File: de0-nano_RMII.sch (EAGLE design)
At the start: 40 parts, among them U1 DP83848, X1 1-227161-2

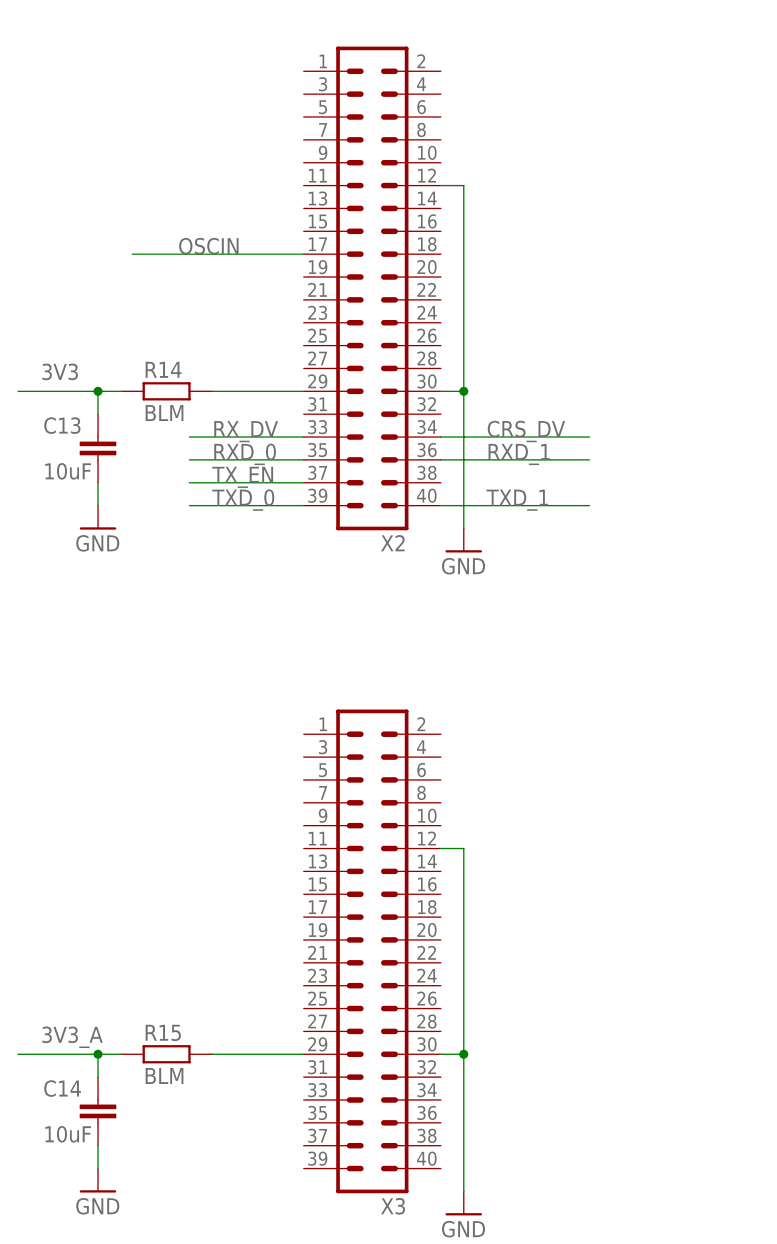
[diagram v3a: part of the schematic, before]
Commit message: removed some pads on connector
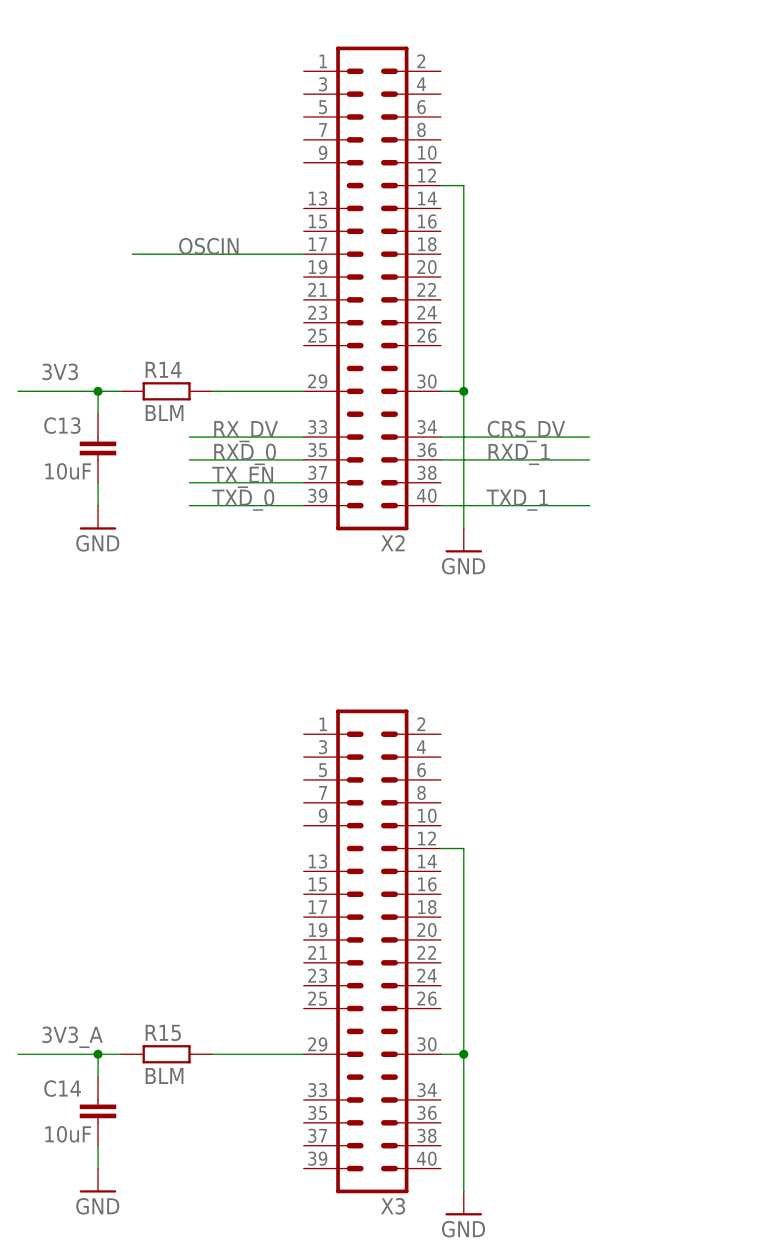
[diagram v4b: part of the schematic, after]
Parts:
- X2, X3: device con-lstb:MA20-2 -> con-lstb:MA20-2_ALT
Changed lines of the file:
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@@
 <?xml version="1.0" encoding="utf-8"?>
 <!DOCTYPE eagle SYSTEM "eagle.dtd">
-<eagle version="7.6.0">
+<eagle version="8.0.2">
 <drawing>
 <settings>
@@
 <setting verticaltext="up"/>
 </settings>
-<grid distance="0.05" unitdist="inch" unit="inch" style="lines" multiple="1" display="no" altdistance="0.01" altunitdist="inch" altunit="inch"/>
+<grid distance="0.1" unitdist="inch" unit="inch" style="lines" multiple="1" display="no" altdistance="0.01" altunitdist="inch" altunit="inch"/>
 <layers>
 <layer number="1" name="Top" color="4" fill="1" visible="no" active="no"/>
@@
 <part name="GND1" library="supply1" deviceset="GND" device=""/>
 <part name="X6" library="con-lstb" deviceset="MA13-2" device=""/>
-<part name="X2" library="con-lstb" deviceset="MA20-2" device=""/>
-<part name="X3" library="con-lstb" deviceset="MA20-2" device=""/>
+<part name="X2" library="con-lstb" deviceset="MA20-2_ALT" device=""/>
+<part name="X3" library="con-lstb" deviceset="MA20-2_ALT" device=""/>
 <part name="X7" library="seeed_connector" deviceset="RJ45-HR911105A" device="-HR911105A"/>
 <part name="U1" library="national-semiconductor" deviceset="DP83848" device=""/>

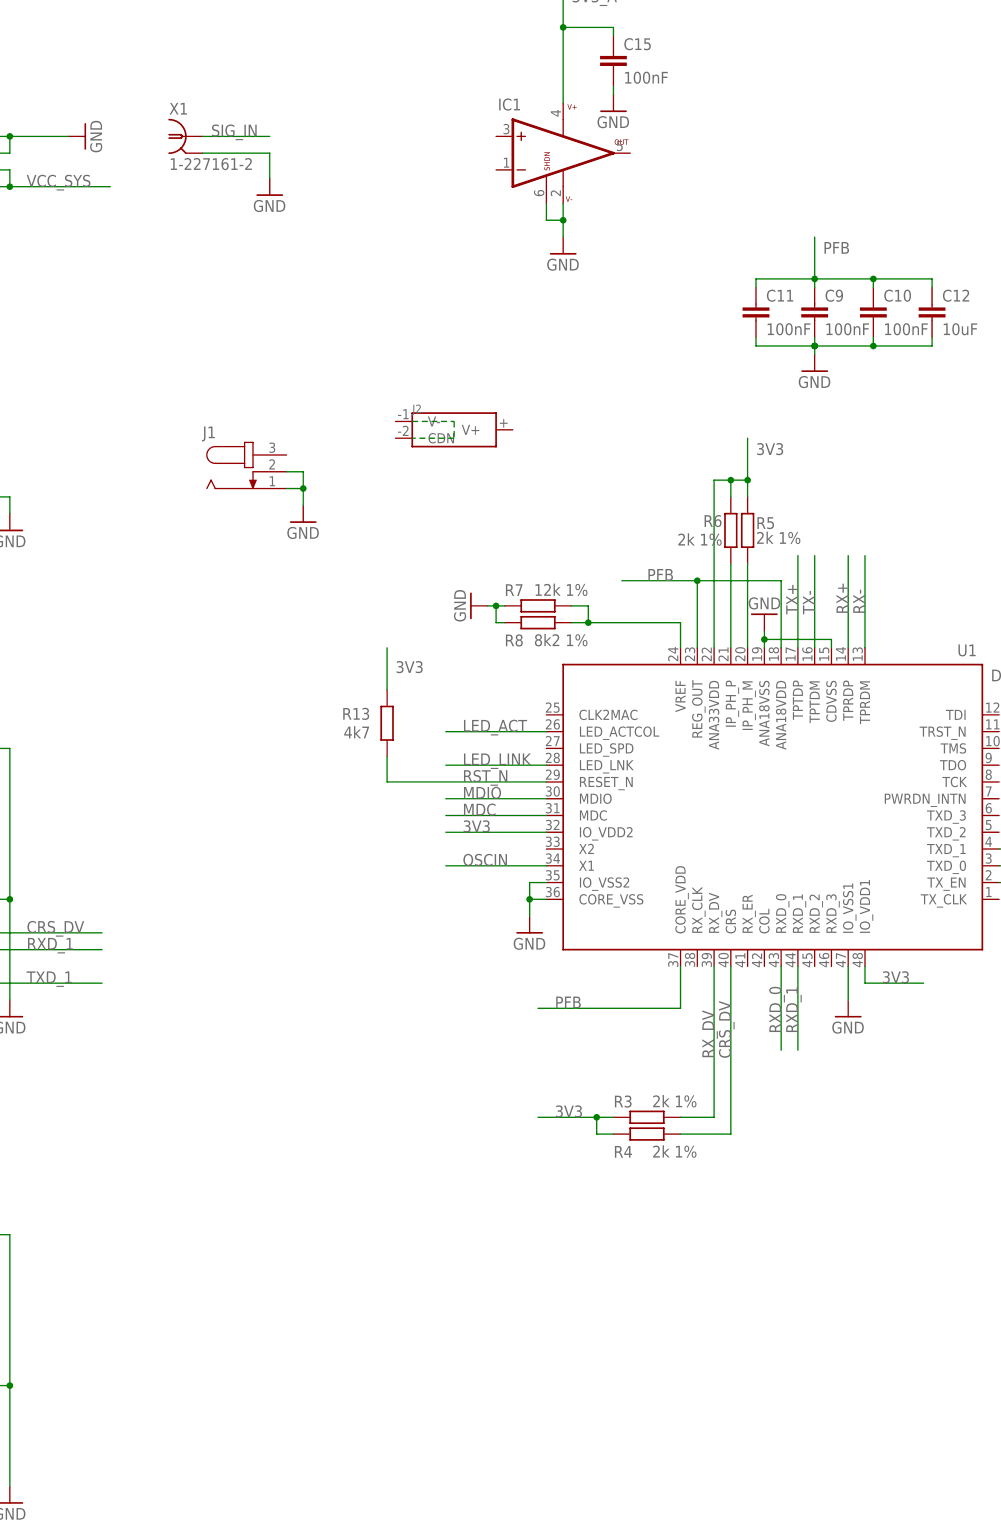
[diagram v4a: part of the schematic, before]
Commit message: added external power and DAC
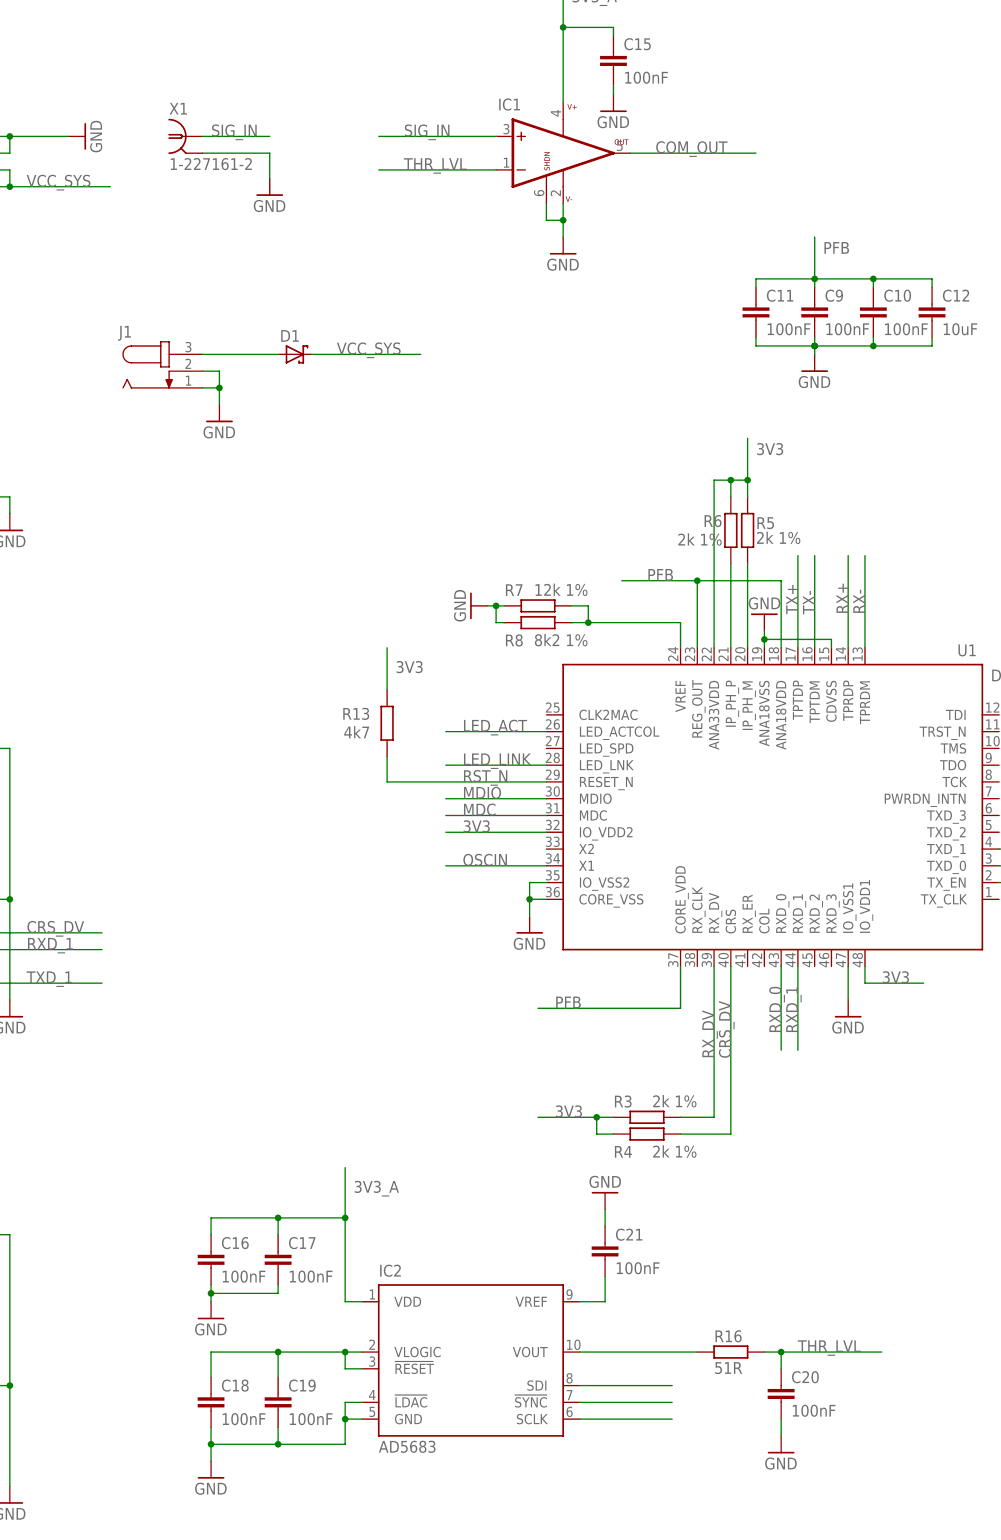
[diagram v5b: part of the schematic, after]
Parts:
- removed J2: (no value), seeed_connector:JACK-3P-2.5MM-2.5MM
- added C16, C17, C18, C19, C20, C21: 100nF, resistor:C-EUC0603
- added D1: (no value), diode:SCHOTTKY-DIODESMC
- added IC2: AD5683, analog-devices:AD5683
- added R16: 51R, resistor:R-EU_R0603
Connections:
- new net COM_OUT: IC1.OUT
- new net N$10: IC2.SDI
- new net N$11: IC2.!SYNC
- new net N$12: IC2.SCLK
- new net N$13: C21.1, IC2.VREF
- new net N$2: C18.1, C19.1, IC2.!RESET, IC2.VLOGIC
- new net N$8: IC2.VOUT, R16.1
- new net THR_LVL: C20.1, IC1.-IN, R16.2
- new net V_RAW: D1.A, J1.3
- net 3V3_A: now also C16.1, C17.1, IC2.VDD
- net GND: now also C16.2, C17.2, C18.2, C19.2, C20.2, C21.2, IC2.!LDAC, IC2.GND
- net SIG_IN: now also IC1.+IN
- net VCC_SYS: now also D1.C
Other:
- moved on the sheet: J1

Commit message: almost done
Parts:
- added R17: 4k7, resistor:R-EU_R0603
- X6: device con-lstb:MA13-2 -> con-lstb:MA13-2_ALT
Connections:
- net N$2 renamed VLOGIC
- removed net N$10: IC2.SDI
- removed net N$11: IC2.!SYNC
- removed net N$12: IC2.SCLK
- new net DAC_CLK: IC2.SCLK, X3.5
- new net DAC_NCS: IC2.!SYNC, R17.2, X3.7
- new net DAC_SDI: IC2.SDI, X3.6
- net 3V3_A: now also R17.1
- net COM_OUT: now also X3.13
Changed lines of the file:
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@@
 <?xml version="1.0" encoding="utf-8"?>
 <!DOCTYPE eagle SYSTEM "eagle.dtd">
-<eagle version="7.6.0">
+<eagle version="8.0.2">
 <drawing>
 <settings>
@@
 <part name="X1" library="con-coax" deviceset="?227161*" device="1-" technology="-2"/>
 <part name="GND1" library="supply1" deviceset="GND" device=""/>
-<part name="X6" library="con-lstb" deviceset="MA13-2" device=""/>
+<part name="X6" library="con-lstb" deviceset="MA13-2_ALT" device=""/>
 <part name="X2" library="con-lstb" deviceset="MA20-2_ALT" device=""/>
 <part name="X3" library="con-lstb" deviceset="MA20-2_ALT" device=""/>
@@
 <part name="C21" library="resistor" deviceset="C-EU" device="C0603" value="100nF"/>
 <part name="GND25" library="supply1" deviceset="GND" device=""/>
+<part name="R17" library="resistor" deviceset="R-EU_" device="R0603" value="4k7"/>
 </parts>
 <sheets>
@@
 </instance>
 <instance part="GND25" gate="1" x="146.05" y="71.12" rot="R180"/>
+<instance part="R17" gate="G$1" x="17.78" y="80.01" smashed="yes" rot="R270">
+<attribute name="NAME" x="15.24" y="82.3214" size="1.778" layer="95" rot="R180"/>
+<attribute name="VALUE" x="15.24" y="79.502" size="1.778" layer="96" rot="R180"/>
+</instance>
 </instances>
 <busses>
@@
 <junction x="106.68" y="67.31"/>
 </segment>
+<segment>
+<pinref part="R17" gate="G$1" pin="1"/>
+<wire x1="17.78" y1="85.09" x2="17.78" y2="93.98" width="0.1524" layer="91"/>
+<label x="19.05" y="88.9" size="1.778" layer="95"/>
+</segment>
 </net>
 <net name="N$1" class="0">
@@
 <label x="153.67" y="228.6" size="1.778" layer="95"/>
 </segment>
+<segment>
+<pinref part="X3" gate="G$1" pin="13"/>
+<wire x1="38.1" y1="62.23" x2="17.78" y2="62.23" width="0.1524" layer="91"/>
+<label x="22.86" y="62.23" size="1.778" layer="95"/>
+</segment>
 </net>
 <net name="V_RAW" class="0">
@@
 </segment>
 </net>
-<net name="N$2" class="0">
+<net name="VLOGIC" class="0">
 <segment>
 <pinref part="IC2" gate="G$1" pin="!RESET"/>
@@
 </segment>
 </net>
-<net name="N$10" class="0">
+<net name="DAC_SDI" class="0">
 <segment>
 <pinref part="IC2" gate="G$1" pin="SDI"/>
-<wire x1="142.24" y1="41.91" x2="156.21" y2="41.91" width="0.1524" layer="91"/>
-</segment>
-</net>
-<net name="N$11" class="0">
+<wire x1="142.24" y1="41.91" x2="158.75" y2="41.91" width="0.1524" layer="91"/>
+<label x="144.78" y="41.91" size="1.778" layer="95"/>
+</segment>
+<segment>
+<pinref part="X3" gate="G$1" pin="6"/>
+<wire x1="53.34" y1="72.39" x2="66.04" y2="72.39" width="0.1524" layer="91"/>
+<label x="55.88" y="72.39" size="1.778" layer="95"/>
+</segment>
+</net>
+<net name="DAC_NCS" class="0">
 <segment>
 <pinref part="IC2" gate="G$1" pin="!SYNC"/>
-<wire x1="142.24" y1="39.37" x2="156.21" y2="39.37" width="0.1524" layer="91"/>
-</segment>
-</net>
-<net name="N$12" class="0">
+<wire x1="142.24" y1="39.37" x2="158.75" y2="39.37" width="0.1524" layer="91"/>
+<label x="144.78" y="39.37" size="1.778" layer="95"/>
+</segment>
+<segment>
+<pinref part="X3" gate="G$1" pin="7"/>
+<wire x1="38.1" y1="69.85" x2="17.78" y2="69.85" width="0.1524" layer="91"/>
+<label x="22.86" y="69.85" size="1.778" layer="95"/>
+<pinref part="R17" gate="G$1" pin="2"/>
+<wire x1="17.78" y1="69.85" x2="17.78" y2="74.93" width="0.1524" layer="91"/>
+</segment>
+</net>
+<net name="DAC_CLK" class="0">
 <segment>
 <pinref part="IC2" gate="G$1" pin="SCLK"/>
-<wire x1="142.24" y1="36.83" x2="156.21" y2="36.83" width="0.1524" layer="91"/>
-</segment>
-</net>
+<wire x1="142.24" y1="36.83" x2="158.75" y2="36.83" width="0.1524" layer="91"/>
+<label x="144.78" y="36.83" size="1.778" layer="95"/>
+</segment>
+<segment>
+<pinref part="X3" gate="G$1" pin="5"/>
+<wire x1="38.1" y1="72.39" x2="20.32" y2="72.39" width="0.1524" layer="91"/>
+<label x="22.86" y="72.39" size="1.778" layer="95"/>
+</segment>
+</net>
